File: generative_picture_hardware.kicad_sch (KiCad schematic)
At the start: 67 parts, among them J1 e_Paper_HAT, J2 Conn_ARM_JTAG_SWD_10, J3 USB_C_Receptacle_USB2.0, Q1 PMN48XP, Q2 DMG9926UDM, Q3 MBT3904DW1, SW1 SW_Push, SW2 SW_Push, U1 AP2112K-3.3, U2 ESP32-WROOM-32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

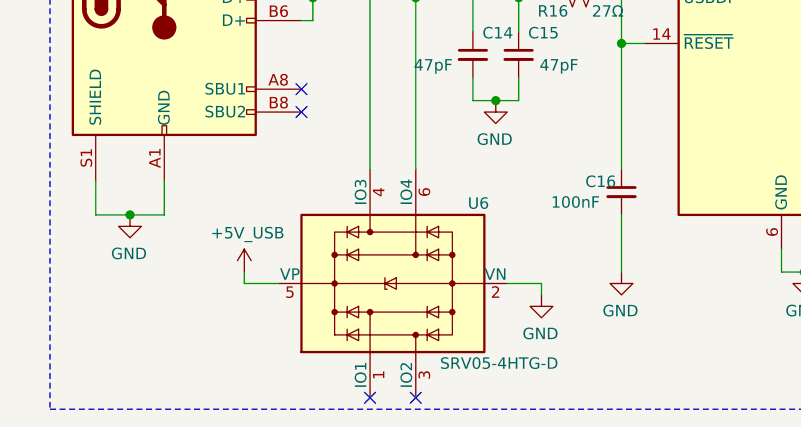
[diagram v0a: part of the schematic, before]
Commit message: Changes pins on the TVS diodes to make it easier to route
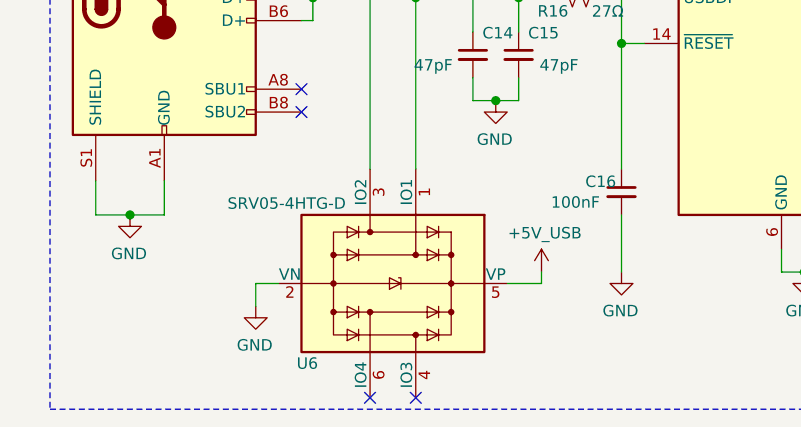
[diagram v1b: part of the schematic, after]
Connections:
- net D+: now also U6.1 (IO1); no longer U6.6 (IO4)
- net D-: now also U6.3 (IO2); no longer U6.4 (IO3)
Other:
- moved on the sheet: U6
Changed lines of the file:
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@@
-    (stroke (width 0) (type solid) (color 0 0 0 0))
-  )
-  (wire (pts (xy 35.56 181.61) (xy 35.56 182.88))
-    (stroke (width 0) (type solid) (color 0 0 0 0))
-  )
-  (wire (pts (xy 35.56 182.88) (xy 39.37 182.88))
     (stroke (width 0) (type solid) (color 0 0 0 0))
   )
@@
     (stroke (width 0) (type solid) (color 0 0 0 0))
   )
+  (wire (pts (xy 36.83 182.88) (xy 36.83 185.42))
+    (stroke (width 0) (type solid) (color 0 0 0 0))
+  )
+  (wire (pts (xy 36.83 182.88) (xy 39.37 182.88))
+    (stroke (width 0) (type solid) (color 0 0 0 0))
+  )
   (wire (pts (xy 41.91 133.35) (xy 44.45 133.35))
     (stroke (width 0) (type solid) (color 0 0 0 0))
@@
     (stroke (width 0) (type solid) (color 0 0 0 0))
   )
-  (wire (pts (xy 68.58 182.88) (xy 68.58 184.15))
+  (wire (pts (xy 68.58 181.61) (xy 68.58 182.88))
     (stroke (width 0) (type solid) (color 0 0 0 0))
   )
@@
     (pin "1")
   )
-  (symbol (lib_id "Generative_picture:+5V_USB") (at 35.56 181.61 0) (unit 1)
-    (in_bom yes) (on_board yes)
-    (property "Reference" "#PWR042" (id 0) (at 35.56 185.42 0)
-      (effects (font (size 1.27 1.27)) hide)
-    )
-    (property "Value" "+5V_USB" (id 1) (at 35.9283 177.2856 0))
-    (property "Footprint" "" (id 2) (at 35.56 181.61 0)
-      (effects (font (size 1.27 1.27)) hide)
-    )
-    (property "Datasheet" "" (id 3) (at 35.56 181.61 0)
-      (effects (font (size 1.27 1.27)) hide)
-    )
-    (pin "1")
-  )
   (symbol (lib_id "power:+3V3") (at 36.83 26.67 0) (unit 1)
     (in_bom yes) (on_board yes)
@@
     (pin "1")
   )
+  (symbol (lib_id "Generative_picture:+5V_USB") (at 68.58 181.61 0) (unit 1)
+    (in_bom yes) (on_board yes)
+    (property "Reference" "#PWR042" (id 0) (at 68.58 185.42 0)
+      (effects (font (size 1.27 1.27)) hide)
+    )
+    (property "Value" "+5V_USB" (id 1) (at 68.9483 177.2856 0))
+    (property "Footprint" "" (id 2) (at 68.58 181.61 0)
+      (effects (font (size 1.27 1.27)) hide)
+    )
+    (property "Datasheet" "" (id 3) (at 68.58 181.61 0)
+      (effects (font (size 1.27 1.27)) hide)
+    )
+    (pin "1")
+  )
   (symbol (lib_id "Generative_picture:+5V_USB") (at 74.93 120.65 0) (unit 1)
     (in_bom yes) (on_board yes)
@@
     (pin "1")
   )
+  (symbol (lib_id "power:GND") (at 36.83 185.42 0) (mirror y) (unit 1)
+    (in_bom yes) (on_board yes)
+    (property "Reference" "#PWR045" (id 0) (at 36.83 191.77 0)
+      (effects (font (size 1.27 1.27)) hide)
+    )
+    (property "Value" "GND" (id 1) (at 36.7157 189.7444 0))
+    (property "Footprint" "" (id 2) (at 36.83 185.42 0)
+      (effects (font (size 1.27 1.27)) hide)
+    )
+    (property "Datasheet" "" (id 3) (at 36.83 185.42 0)
+      (effects (font (size 1.27 1.27)) hide)
+    )
+    (pin "1")
+  )
   (symbol (lib_id "power:GND") (at 59.69 137.16 0) (mirror y) (unit 1)
     (in_bom yes) (on_board yes)
@@
     )
     (property "Datasheet" "" (id 3) (at 66.04 101.6 0)
-      (effects (font (size 1.27 1.27)) hide)
-    )
-    (pin "1")
-  )
-  (symbol (lib_id "power:GND") (at 68.58 184.15 0) (mirror y) (unit 1)
-    (in_bom yes) (on_board yes)
-    (property "Reference" "#PWR045" (id 0) (at 68.58 190.5 0)
-      (effects (font (size 1.27 1.27)) hide)
-    )
-    (property "Value" "GND" (id 1) (at 68.4657 188.4744 0))
-    (property "Footprint" "" (id 2) (at 68.58 184.15 0)
-      (effects (font (size 1.27 1.27)) hide)
-    )
-    (property "Datasheet" "" (id 3) (at 68.58 184.15 0)
       (effects (font (size 1.27 1.27)) hide)
     )
@@
     (pin "6")
   )
-  (symbol (lib_id "Power_Protection:SRV05-4") (at 52.07 182.88 90) (unit 1)
-    (in_bom yes) (on_board yes)
-    (property "Reference" "U6" (id 0) (at 61.5758 173.99 90))
-    (property "Value" "SRV05-4HTG-D" (id 1) (at 63.875 191.77 90))
-    (property "Footprint" "Package_TO_SOT_SMD:SOT-23-6" (id 2) (at 63.5 165.1 0)
-      (effects (font (size 1.27 1.27)) hide)
-    )
+  (symbol (lib_id "Power_Protection:SRV05-4") (at 52.07 182.88 270) (unit 1)
+    (in_bom yes) (on_board yes)
+    (property "Reference" "U6" (id 0) (at 42.5642 191.77 90))
+    (property "Value" "SRV05-4HTG-D" (id 1) (at 40.265 173.99 90))
+    (property "Footprint" "Package_TO_SOT_SMD:SOT-23-6" (id 2) (at 40.64 200.66 0)
+      (effects (font (size 1.27 1.27)) hide)
+    )

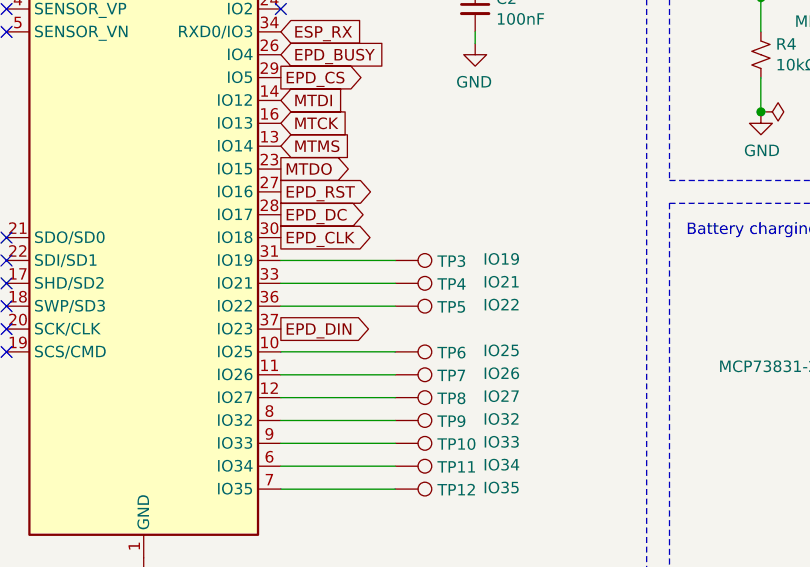
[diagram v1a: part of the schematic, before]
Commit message: Removes some unused test points
They have no immediate use and wouldn't be trivial to route.
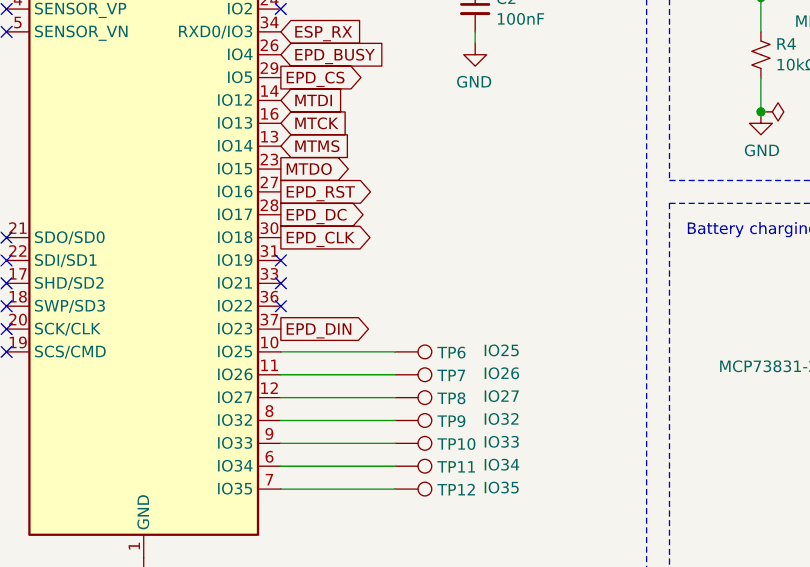
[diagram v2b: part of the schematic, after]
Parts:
- removed TP3: IO19, TestPoint:TestPoint_Pad_D2.0mm, symbol Connector:TestPoint
- removed TP4: IO21, TestPoint:TestPoint_Pad_D2.0mm, symbol Connector:TestPoint
- removed TP5: IO22, TestPoint:TestPoint_Pad_D2.0mm, symbol Connector:TestPoint
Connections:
- no-connect marks 46 -> 49
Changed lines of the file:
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@@
   (no_connect (at 54.61 195.58))
   (no_connect (at 81.28 40.64))
+  (no_connect (at 81.28 68.58))
+  (no_connect (at 81.28 71.12))
+  (no_connect (at 81.28 73.66))
   (no_connect (at 115.57 148.59))
   (no_connect (at 115.57 153.67))
@@
     (stroke (width 0) (type solid) (color 0 0 0 0))
   )
-  (wire (pts (xy 81.28 68.58) (xy 93.98 68.58))
-    (stroke (width 0) (type solid) (color 0 0 0 0))
-  )
-  (wire (pts (xy 81.28 71.12) (xy 93.98 71.12))
-    (stroke (width 0) (type solid) (color 0 0 0 0))
-  )
-  (wire (pts (xy 81.28 73.66) (xy 93.98 73.66))
-    (stroke (width 0) (type solid) (color 0 0 0 0))
-  )
   (wire (pts (xy 81.28 78.74) (xy 93.98 78.74))
     (stroke (width 0) (type solid) (color 0 0 0 0))
@@
     (pin "1")
   )
-  (symbol (lib_id "Connector:TestPoint") (at 93.98 68.58 270) (unit 1)
-    (in_bom yes) (on_board yes)
-    (property "Reference" "TP3" (id 0) (at 98.6791 68.7006 90)
-      (effects (font (size 1.27 1.27)) (justify left))
-    )
-    (property "Value" "IO19" (id 1) (at 103.759 68.459 90)
-      (effects (font (size 1.27 1.27)) (justify left))
-    )
-    (property "Footprint" "TestPoint:TestPoint_Pad_D2.0mm" (id 2) (at 93.98 73.66 0)
-      (effects (font (size 1.27 1.27)) hide)
-    )
-    (property "Datasheet" "~" (id 3) (at 93.98 73.66 0)
-      (effects (font (size 1.27 1.27)) hide)
-    )
-    (pin "1")
-  )
-  (symbol (lib_id "Connector:TestPoint") (at 93.98 71.12 270) (unit 1)
-    (in_bom yes) (on_board yes)
-    (property "Reference" "TP4" (id 0) (at 98.6791 71.2406 90)
-      (effects (font (size 1.27 1.27)) (justify left))
-    )
-    (property "Value" "IO21" (id 1) (at 103.759 70.999 90)
-      (effects (font (size 1.27 1.27)) (justify left))
-    )
-    (property "Footprint" "TestPoint:TestPoint_Pad_D2.0mm" (id 2) (at 93.98 76.2 0)
-      (effects (font (size 1.27 1.27)) hide)
-    )
-    (property "Datasheet" "~" (id 3) (at 93.98 76.2 0)
-      (effects (font (size 1.27 1.27)) hide)
-    )
-    (pin "1")
-  )
-  (symbol (lib_id "Connector:TestPoint") (at 93.98 73.66 270) (unit 1)
-    (in_bom yes) (on_board yes)
-    (property "Reference" "TP5" (id 0) (at 98.6791 73.7806 90)
-      (effects (font (size 1.27 1.27)) (justify left))
-    )
-    (property "Value" "IO22" (id 1) (at 103.759 73.539 90)
-      (effects (font (size 1.27 1.27)) (justify left))
-    )
-    (property "Footprint" "TestPoint:TestPoint_Pad_D2.0mm" (id 2) (at 93.98 78.74 0)
-      (effects (font (size 1.27 1.27)) hide)
-    )
-    (property "Datasheet" "~" (id 3) (at 93.98 78.74 0)
-      (effects (font (size 1.27 1.27)) hide)
-    )
-    (pin "1")
-  )
   (symbol (lib_id "Connector:TestPoint") (at 93.98 78.74 270) (unit 1)
     (in_bom yes) (on_board yes)
@@
       (reference "TP2") (unit 1) (value "bat -") (footprint "TestPoint:TestPoint_Pad_D2.0mm")
     )
-    (path "/d72e2e00-166f-46a4-b676-a9596746b0bd"
-      (reference "TP3") (unit 1) (value "IO19") (footprint "TestPoint:TestPoint_Pad_D2.0mm")
-    )
-    (path "/93e407d8-f449-49f3-bc49-49b1d072a848"
-      (reference "TP4") (unit 1) (value "IO21") (footprint "TestPoint:TestPoint_Pad_D2.0mm")
-    )
-    (path "/7b8a980e-33b6-435b-af52-b95a34ba2a1f"
-      (reference "TP5") (unit 1) (value "IO22") (footprint "TestPoint:TestPoint_Pad_D2.0mm")
-    )
     (path "/270f2b79-8713-40da-ba21-2980f9dd1244"

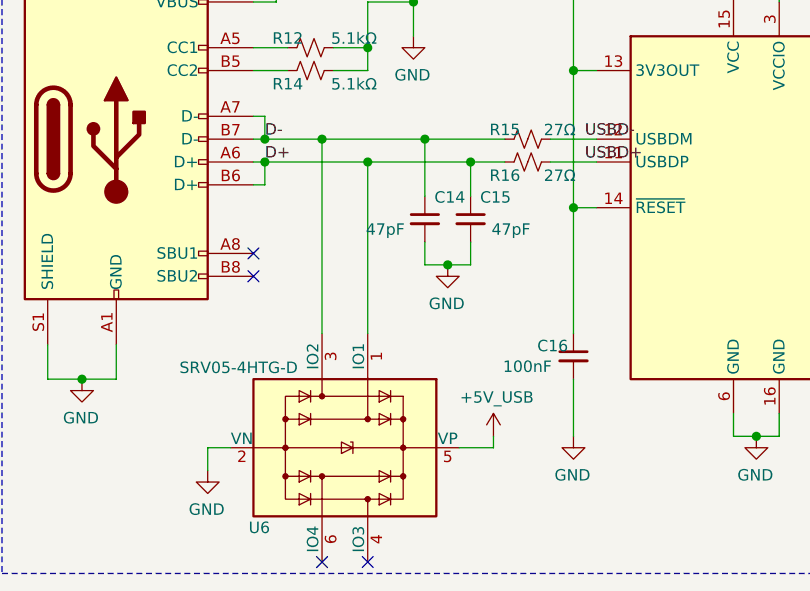
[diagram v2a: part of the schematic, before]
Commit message: Reroutes TVS diodes in USB line
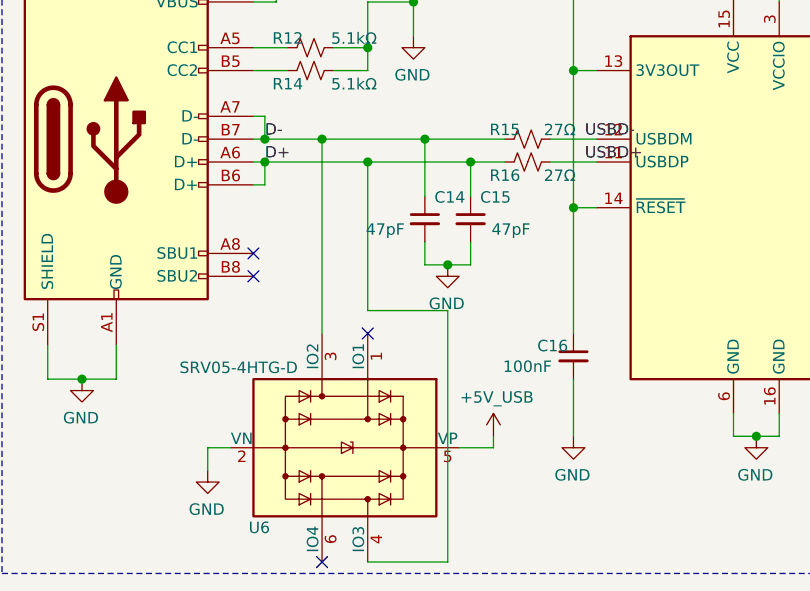
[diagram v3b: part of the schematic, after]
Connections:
- net D+: now also U6.4 (IO3); no longer U6.1 (IO1)
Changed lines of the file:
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@@
   (no_connect (at 50.8 76.2))
   (no_connect (at 50.8 78.74))
-  (no_connect (at 54.61 195.58))
+  (no_connect (at 54.61 170.18))
   (no_connect (at 81.28 40.64))
   (no_connect (at 81.28 68.58))
@@
     (stroke (width 0) (type solid) (color 0 0 0 0))
   )
-  (wire (pts (xy 54.61 151.13) (xy 54.61 170.18))
+  (wire (pts (xy 54.61 151.13) (xy 54.61 167.64))
     (stroke (width 0) (type solid) (color 0 0 0 0))
   )
@@
     (stroke (width 0) (type solid) (color 0 0 0 0))
   )
+  (wire (pts (xy 54.61 167.64) (xy 63.5 167.64))
+    (stroke (width 0) (type solid) (color 0 0 0 0))
+  )
   (wire (pts (xy 59.69 123.19) (xy 59.69 125.73))
     (stroke (width 0) (type solid) (color 0 0 0 0))
@@
     (stroke (width 0) (type solid) (color 0 0 0 0))
   )
+  (wire (pts (xy 63.5 167.64) (xy 63.5 195.58))
+    (stroke (width 0) (type solid) (color 0 0 0 0))
+  )
+  (wire (pts (xy 63.5 195.58) (xy 54.61 195.58))
+    (stroke (width 0) (type solid) (color 0 0 0 0))
+  )

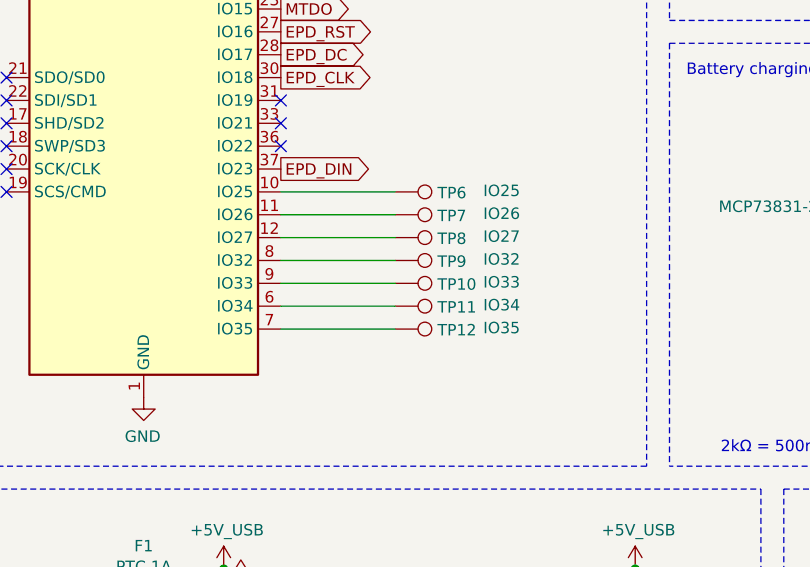
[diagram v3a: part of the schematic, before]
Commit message: Removes some more test points for GPIO pins
I don't really have any use planned for them. Two should be plenty if
needed at all.
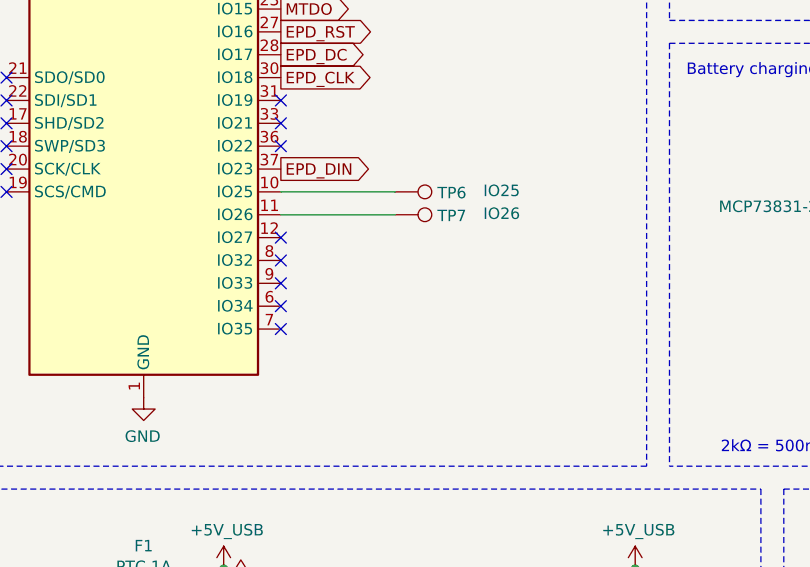
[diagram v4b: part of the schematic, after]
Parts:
- removed TP10: IO33, TestPoint:TestPoint_Pad_D2.0mm, symbol Connector:TestPoint
- removed TP11: IO34, TestPoint:TestPoint_Pad_D2.0mm, symbol Connector:TestPoint
- removed TP12: IO35, TestPoint:TestPoint_Pad_D2.0mm, symbol Connector:TestPoint
- removed TP8: IO27, TestPoint:TestPoint_Pad_D2.0mm, symbol Connector:TestPoint
- removed TP9: IO32, TestPoint:TestPoint_Pad_D2.0mm, symbol Connector:TestPoint
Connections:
- no-connect marks 49 -> 54
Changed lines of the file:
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@@
   (no_connect (at 81.28 71.12))
   (no_connect (at 81.28 73.66))
+  (no_connect (at 81.28 83.82))
+  (no_connect (at 81.28 86.36))
+  (no_connect (at 81.28 88.9))
+  (no_connect (at 81.28 91.44))
+  (no_connect (at 81.28 93.98))
   (no_connect (at 115.57 148.59))
   (no_connect (at 115.57 153.67))
@@
     (stroke (width 0) (type solid) (color 0 0 0 0))
   )
-  (wire (pts (xy 81.28 83.82) (xy 93.98 83.82))
-    (stroke (width 0) (type solid) (color 0 0 0 0))
-  )
-  (wire (pts (xy 81.28 86.36) (xy 93.98 86.36))
-    (stroke (width 0) (type solid) (color 0 0 0 0))
-  )
-  (wire (pts (xy 81.28 88.9) (xy 93.98 88.9))
-    (stroke (width 0) (type solid) (color 0 0 0 0))
-  )
-  (wire (pts (xy 81.28 91.44) (xy 93.98 91.44))
-    (stroke (width 0) (type solid) (color 0 0 0 0))
-  )
-  (wire (pts (xy 81.28 93.98) (xy 93.98 93.98))
-    (stroke (width 0) (type solid) (color 0 0 0 0))
-  )
   (wire (pts (xy 95.25 179.07) (xy 95.25 181.61))
     (stroke (width 0) (type solid) (color 0 0 0 0))
@@
     (pin "1")
   )
-  (symbol (lib_id "Connector:TestPoint") (at 93.98 83.82 270) (unit 1)
-    (in_bom yes) (on_board yes)
-    (property "Reference" "TP8" (id 0) (at 98.6791 83.9406 90)
-      (effects (font (size 1.27 1.27)) (justify left))
-    )
-    (property "Value" "IO27" (id 1) (at 103.759 83.699 90)
-      (effects (font (size 1.27 1.27)) (justify left))
-    )
-    (property "Footprint" "TestPoint:TestPoint_Pad_D2.0mm" (id 2) (at 93.98 88.9 0)
-      (effects (font (size 1.27 1.27)) hide)
-    )
-    (property "Datasheet" "~" (id 3) (at 93.98 88.9 0)
-      (effects (font (size 1.27 1.27)) hide)
-    )
-    (pin "1")
-  )
-  (symbol (lib_id "Connector:TestPoint") (at 93.98 86.36 270) (unit 1)
-    (in_bom yes) (on_board yes)
-    (property "Reference" "TP9" (id 0) (at 98.6791 86.4806 90)
-      (effects (font (size 1.27 1.27)) (justify left))
-    )
-    (property "Value" "IO32" (id 1) (at 103.759 86.239 90)
-      (effects (font (size 1.27 1.27)) (justify left))
-    )
-    (property "Footprint" "TestPoint:TestPoint_Pad_D2.0mm" (id 2) (at 93.98 91.44 0)
-      (effects (font (size 1.27 1.27)) hide)
-    )
-    (property "Datasheet" "~" (id 3) (at 93.98 91.44 0)
-      (effects (font (size 1.27 1.27)) hide)
-    )
-    (pin "1")
-  )
-  (symbol (lib_id "Connector:TestPoint") (at 93.98 88.9 270) (unit 1)
-    (in_bom yes) (on_board yes)
-    (property "Reference" "TP10" (id 0) (at 98.6791 89.0206 90)
-      (effects (font (size 1.27 1.27)) (justify left))
-    )
-    (property "Value" "IO33" (id 1) (at 103.759 88.779 90)
-      (effects (font (size 1.27 1.27)) (justify left))
-    )
-    (property "Footprint" "TestPoint:TestPoint_Pad_D2.0mm" (id 2) (at 93.98 93.98 0)
-      (effects (font (size 1.27 1.27)) hide)
-    )
-    (property "Datasheet" "~" (id 3) (at 93.98 93.98 0)
-      (effects (font (size 1.27 1.27)) hide)
-    )
-    (pin "1")
-  )
-  (symbol (lib_id "Connector:TestPoint") (at 93.98 91.44 270) (unit 1)
-    (in_bom yes) (on_board yes)
-    (property "Reference" "TP11" (id 0) (at 98.6791 91.5606 90)
-      (effects (font (size 1.27 1.27)) (justify left))
-    )
-    (property "Value" "IO34" (id 1) (at 103.759 91.319 90)
-      (effects (font (size 1.27 1.27)) (justify left))
-    )
-    (property "Footprint" "TestPoint:TestPoint_Pad_D2.0mm" (id 2) (at 93.98 96.52 0)
-      (effects (font (size 1.27 1.27)) hide)
-    )
-    (property "Datasheet" "~" (id 3) (at 93.98 96.52 0)
-      (effects (font (size 1.27 1.27)) hide)
-    )
-    (pin "1")
-  )
-  (symbol (lib_id "Connector:TestPoint") (at 93.98 93.98 270) (unit 1)
-    (in_bom yes) (on_board yes)
-    (property "Reference" "TP12" (id 0) (at 98.6791 94.1006 90)
-      (effects (font (size 1.27 1.27)) (justify left))
-    )
-    (property "Value" "IO35" (id 1) (at 103.759 93.859 90)
-      (effects (font (size 1.27 1.27)) (justify left))
-    )
-    (property "Footprint" "TestPoint:TestPoint_Pad_D2.0mm" (id 2) (at 93.98 99.06 0)
-      (effects (font (size 1.27 1.27)) hide)
-    )
-    (property "Datasheet" "~" (id 3) (at 93.98 99.06 0)
-      (effects (font (size 1.27 1.27)) hide)
-    )
-    (pin "1")
-  )
   (symbol (lib_id "Connector:TestPoint") (at 142.24 125.73 90) (unit 1)
     (in_bom yes) (on_board yes)
@@
       (reference "TP7") (unit 1) (value "IO26") (footprint "TestPoint:TestPoint_Pad_D2.0mm")
     )
-    (path "/ff9e7c25-fd02-469f-bd50-a6868ff4c8b1"
-      (reference "TP8") (unit 1) (value "IO27") (footprint "TestPoint:TestPoint_Pad_D2.0mm")
-    )
-    (path "/5a2c1981-279a-493b-a0f3-5e603595d1d6"
-      (reference "TP9") (unit 1) (value "IO32") (footprint "TestPoint:TestPoint_Pad_D2.0mm")
-    )
-    (path "/0818096d-4d51-41ad-897f-def87ec52b11"
-      (reference "TP10") (unit 1) (value "IO33") (footprint "TestPoint:TestPoint_Pad_D2.0mm")
-    )
-    (path "/84505109-b578-4492-a990-6aa51e85d959"
-      (reference "TP11") (unit 1) (value "IO34") (footprint "TestPoint:TestPoint_Pad_D2.0mm")
-    )
-    (path "/a70377e0-bdab-45c4-8047-36229c87f09f"
-      (reference "TP12") (unit 1) (value "IO35") (footprint "TestPoint:TestPoint_Pad_D2.0mm")
-    )
     (path "/718b170d-b1ce-42f5-b372-474f1687d990"
